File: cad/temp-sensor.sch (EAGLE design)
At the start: 69 parts, among them Q1 300S14-U, Q2 320S14-U, Q3 320S14-U, U1 SE555D, U2 SE555D, U4 MCP6001UT-I/OT, U5 MCP6001UT-I/OT, U6 MCP6001UT-I/OT, U7 MCP6001UT-I/OT, U8 NCV4264-2CST50T3G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

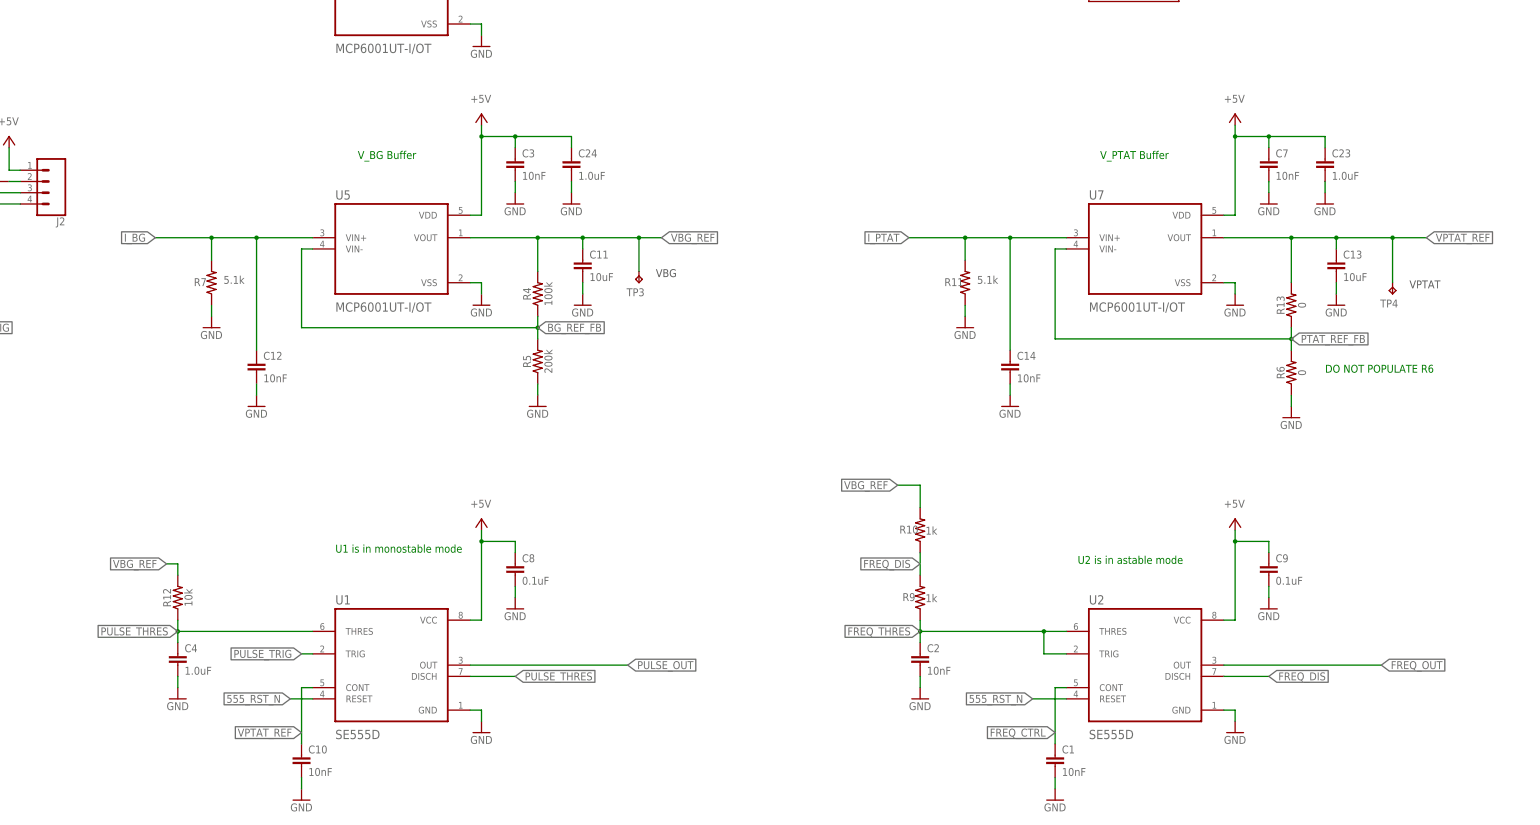
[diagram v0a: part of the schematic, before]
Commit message: Presentation comments
Removed V_BG buffer. Now feeding I_BG current source to input capacitor of monostable timer. Rerouted with 6 mil traces.
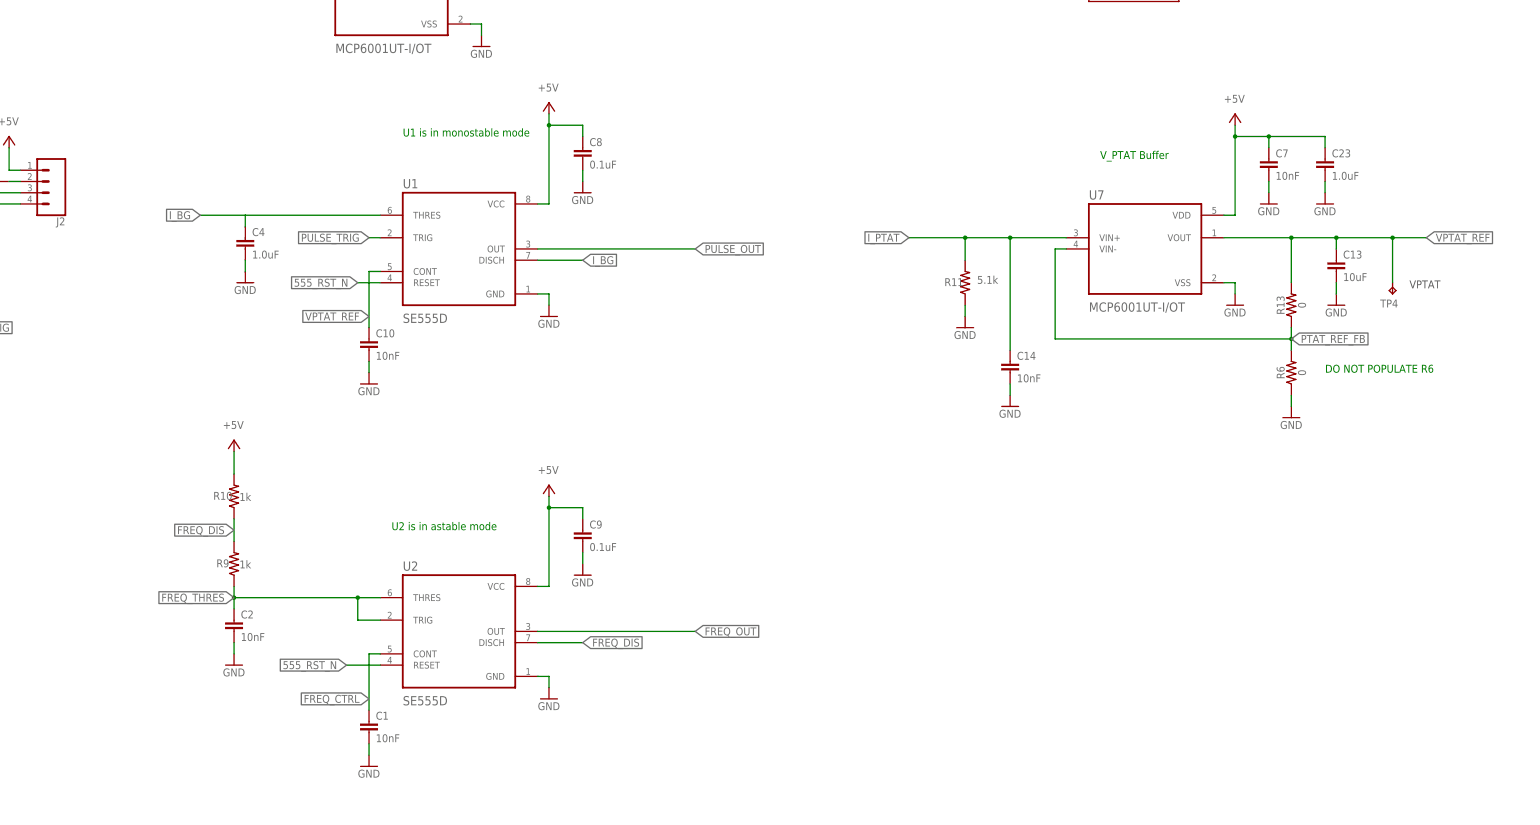
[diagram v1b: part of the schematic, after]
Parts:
- removed C11: 10uF, SparkFun-Capacitors:10UF-0805-25V-10%
- removed C12, C3: 10nF, SparkFun-Capacitors:10NF-0603-50V-10%
- removed C24: 1.0uF, SparkFun-Capacitors:1.0UF-0603-16V-10%-X7R
- removed R12: 10k, SparkFun-Resistors:10KOHM-0603-1/10W-1%
- removed R4: 100k, SparkFun-Resistors:100KOHM-0603-1/10W-1%
- removed R5: 200k, SparkFun-Resistors:200KOHM-0603-1/10W-1%
- removed R7: 5.1k, SparkFun-Resistors:5.1KOHM5.1KOHM-0603-1/10W-1%
- removed TP3: TPPAD1-13, testpad:TPPAD1-13
- removed U5: MCP6001UT-I/OT, MCP6001UT-I_OT:MCP6001UT-I/OT
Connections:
- removed net BG_REF_FB: R4.1, R5.2, U5.VIN-
- removed net PULSE_THRES: C4.1, R12.1, U1.DISCH, U1.THRES
- removed net VBG_REF: C11.1, R10.2, R12.2, R4.2, TP3.TP, U5.VOUT
- net +5V: now also R10.2; no longer C24.1, C3.1, U5.VDD
- net GND: no longer C11.2, C12.2, C24.2, C3.2, R5.1, R7.1, U5.VSS
- net I_BG: now also C4.1, U1.DISCH, U1.THRES; no longer C12.1, R7.2, U5.VIN+
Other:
- note removed: "V_BG Buffer"
- moved on the sheet: C1, C10, C2, C4, C8, C9, R10, R9, U1, U2

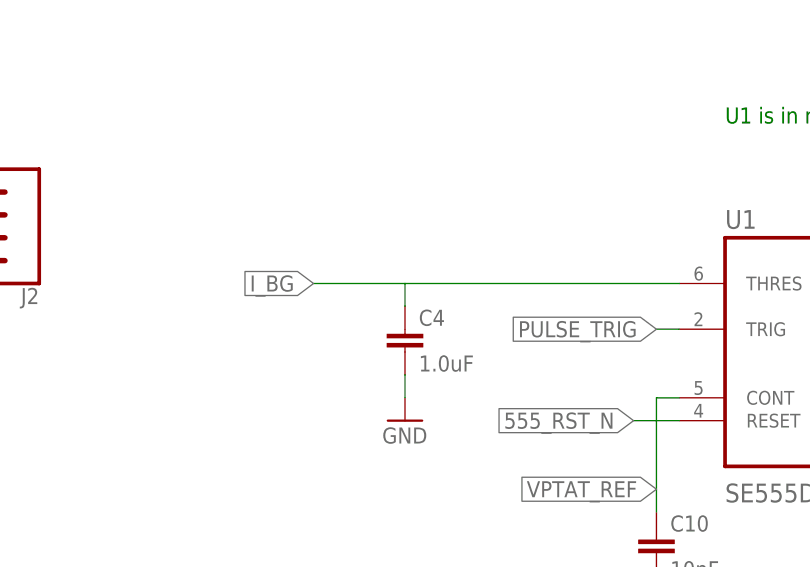
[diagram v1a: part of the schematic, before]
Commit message: Changes from midterm presentation
Changes from midterm presentation including feeding mono stable timer with bandgap current source and a capacitor. This produces a linear voltage since Ic = C dV/dt.
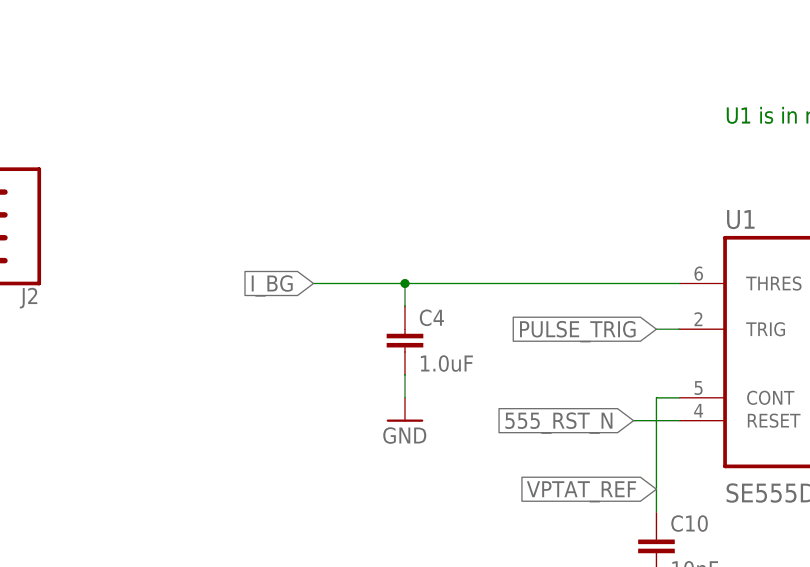
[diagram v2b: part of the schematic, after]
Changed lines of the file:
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@@
 <pinref part="U1" gate="G$1" pin="THRES"/>
 <wire x1="15.24" y1="119.38" x2="5.08" y2="119.38" width="0.1524" layer="91"/>
+<junction x="15.24" y="119.38"/>
 </segment>
 <segment>

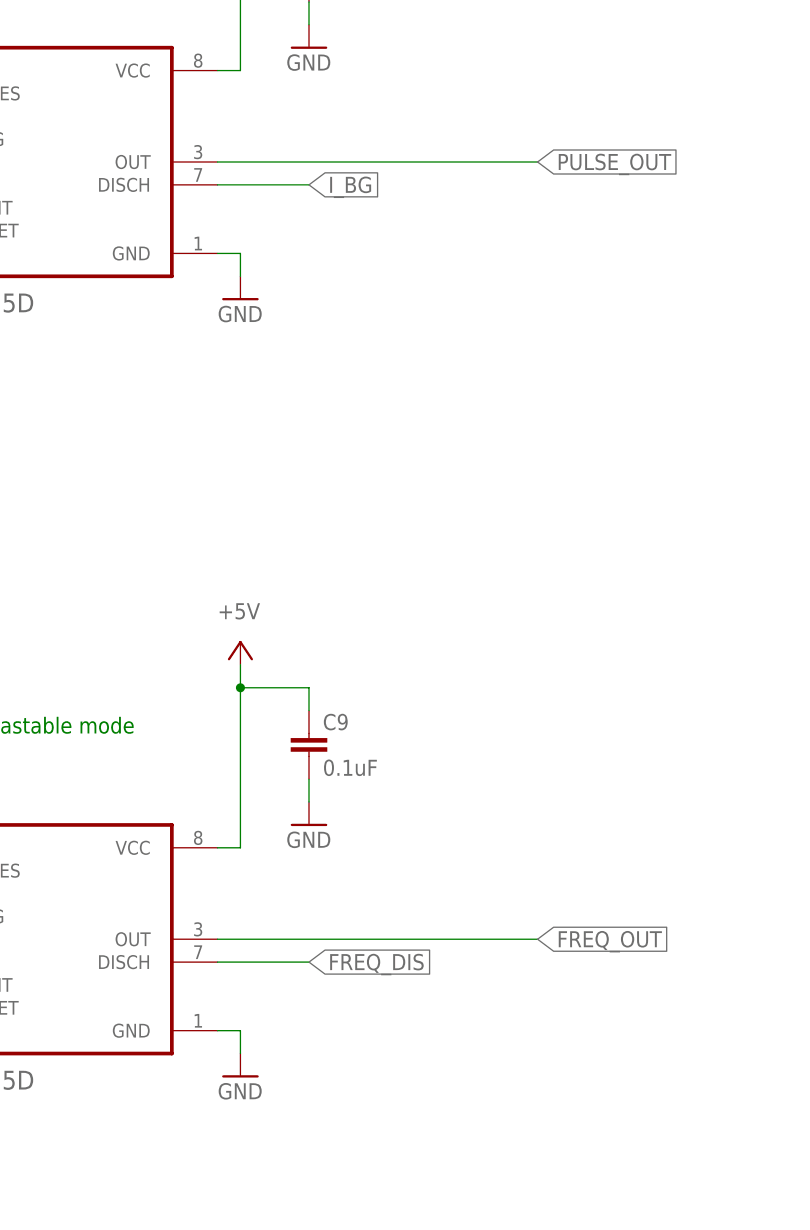
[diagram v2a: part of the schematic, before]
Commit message: Layout change for exposed copper pad
Removed the vias and routing under Q1, Q2, Q3 matched transistors to make space for a thermally conductive exposed copper pad
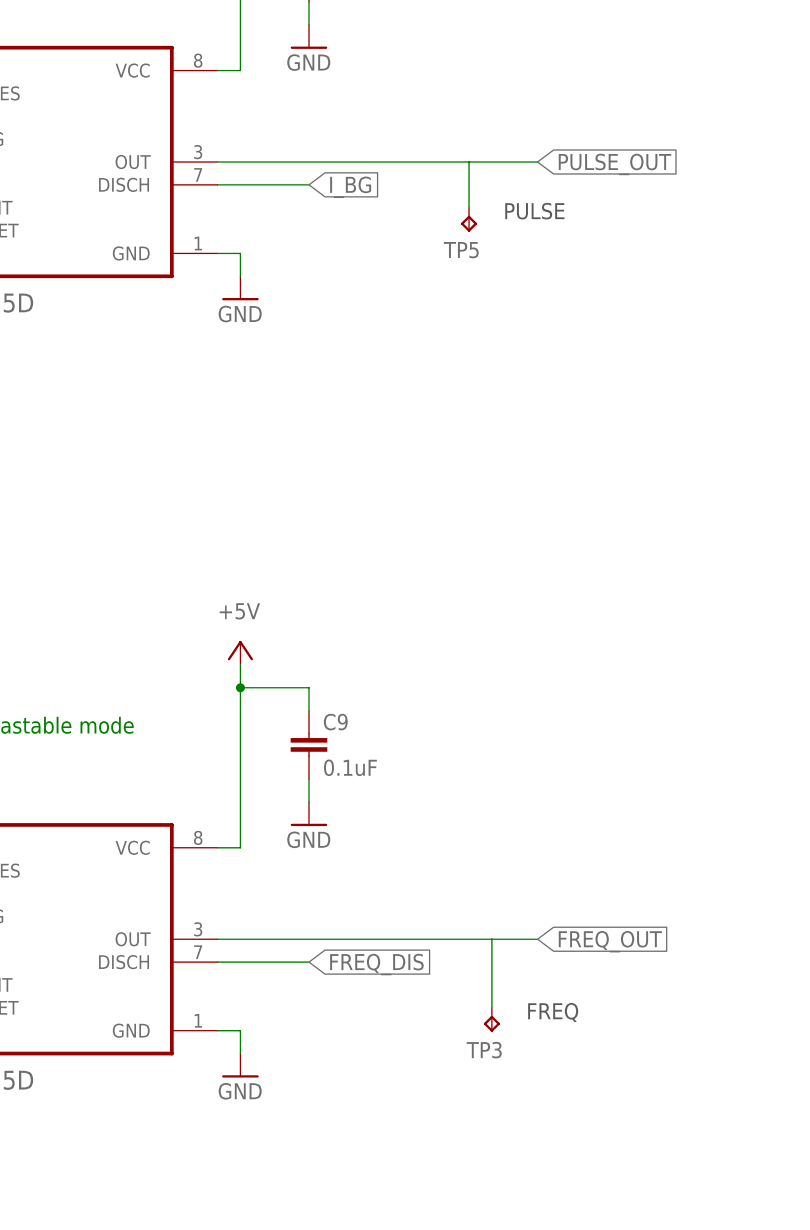
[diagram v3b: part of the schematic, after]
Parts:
- added TP3, TP5: TPPAD1-13, testpad:TPPAD1-13
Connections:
- net FREQ_OUT: now also TP3.TP
- net PULSE_OUT: now also TP5.TP
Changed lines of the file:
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@@
 <part name="GND49" library="supply1" library_urn="urn:adsk.eagle:library:371" deviceset="GND" device=""/>
 <part name="P+3" library="supply1" library_urn="urn:adsk.eagle:library:371" deviceset="+5V" device=""/>
+<part name="TP3" library="testpad" library_urn="urn:adsk.eagle:library:385" deviceset="TP" device="PAD1-13" package3d_urn="urn:adsk.eagle:package:27946/1" value="TPPAD1-13">
+<attribute name="TP_SIGNAL_NAME" value="FREQ"/>
+</part>
+<part name="TP5" library="testpad" library_urn="urn:adsk.eagle:library:385" deviceset="TP" device="PAD1-13" package3d_urn="urn:adsk.eagle:package:27946/1" value="TPPAD1-13">
+<attribute name="TP_SIGNAL_NAME" value="PULSE"/>
+</part>
 </parts>
 <sheets>
@@
 <attribute name="VALUE" x="10.16" y="71.12" size="1.778" layer="96"/>
 </instance>
+<instance part="TP3" gate="G$1" x="111.76" y="15.24" smashed="yes" rot="R180">
+<attribute name="NAME" x="113.03" y="13.97" size="1.778" layer="95" rot="R180"/>
+<attribute name="TP_SIGNAL_NAME" x="115.57" y="16.51" size="1.778" layer="97"/>
+</instance>
+<instance part="TP5" gate="G$1" x="109.22" y="104.14" smashed="yes" rot="R180">
+<attribute name="NAME" x="110.49" y="102.87" size="1.778" layer="95" rot="R180"/>
+<attribute name="TP_SIGNAL_NAME" x="113.03" y="105.41" size="1.778" layer="97"/>
+</instance>
 </instances>
 <busses>
@@
 <net name="PULSE_OUT" class="0">
 <segment>
-<wire x1="81.28" y1="111.76" x2="116.84" y2="111.76" width="0.1524" layer="91"/>
+<wire x1="81.28" y1="111.76" x2="109.22" y2="111.76" width="0.1524" layer="91"/>
 <label x="116.84" y="111.76" size="1.778" layer="95" xref="yes"/>
 <pinref part="U1" gate="G$1" pin="OUT"/>
+<pinref part="TP5" gate="G$1" pin="TP"/>
+<wire x1="109.22" y1="111.76" x2="116.84" y2="111.76" width="0.1524" layer="91"/>
+<wire x1="109.22" y1="106.68" x2="109.22" y2="111.76" width="0.1524" layer="91"/>
 </segment>
 <segment>
@@
 <net name="FREQ_OUT" class="0">
 <segment>
-<wire x1="81.28" y1="25.4" x2="116.84" y2="25.4" width="0.1524" layer="91"/>
+<wire x1="81.28" y1="25.4" x2="111.76" y2="25.4" width="0.1524" layer="91"/>
 <label x="116.84" y="25.4" size="1.778" layer="95" xref="yes"/>
 <pinref part="U2" gate="G$1" pin="OUT"/>
-</segment>
-<segment>
+<pinref part="TP3" gate="G$1" pin="TP"/>
+<wire x1="111.76" y1="25.4" x2="116.84" y2="25.4" width="0.1524" layer="91"/>
+<wire x1="111.76" y1="17.78" x2="111.76" y2="25.4" width="0.1524" layer="91"/>
+</segment>
+<segment>
